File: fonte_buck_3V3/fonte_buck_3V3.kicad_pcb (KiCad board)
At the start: 2 copper layers, 6 parts, among them U1 LM2594M-3.3

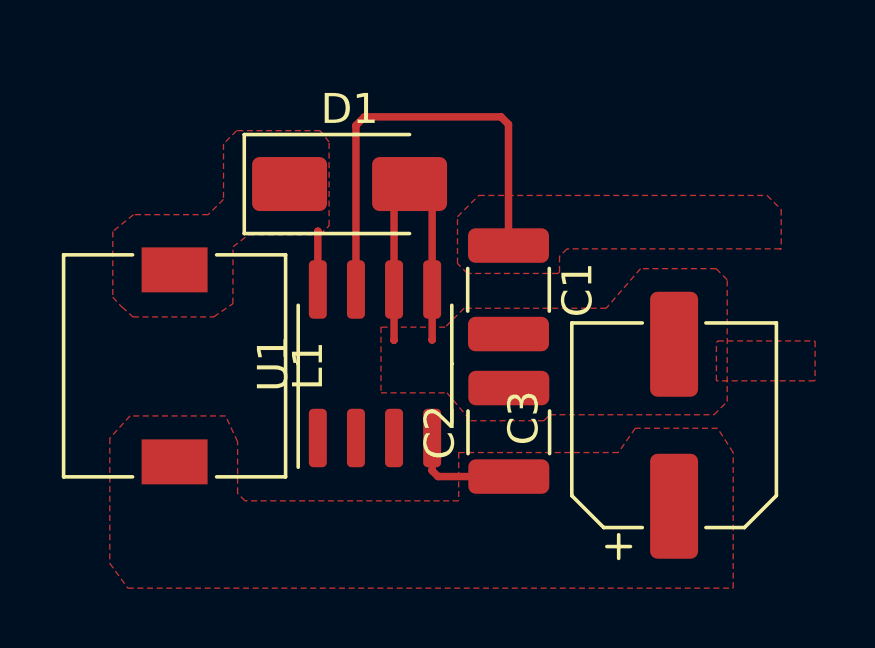
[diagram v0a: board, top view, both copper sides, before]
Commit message: changes in stm and add can module
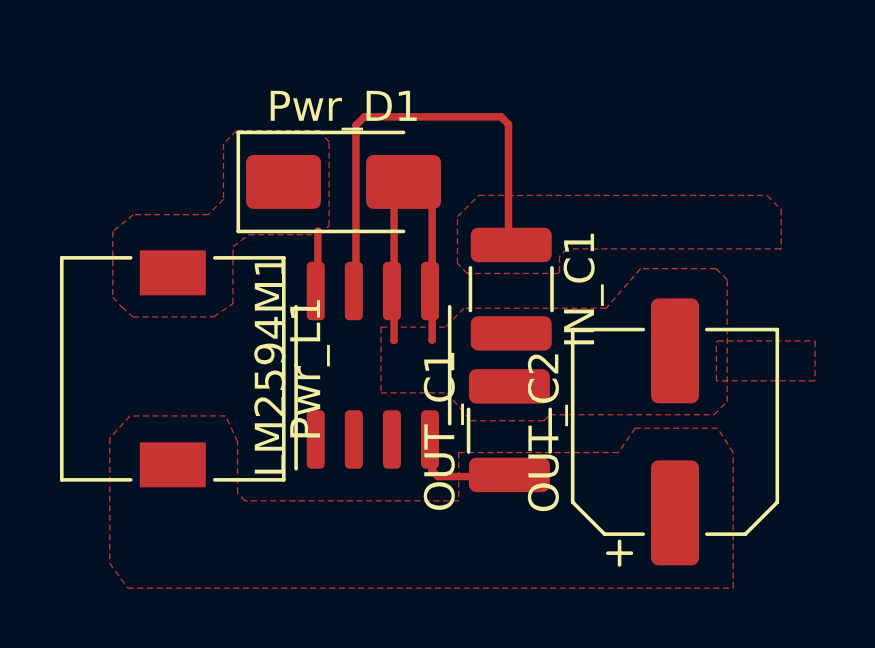
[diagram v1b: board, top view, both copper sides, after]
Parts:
- removed C1: 10uF, Capacitor_SMD:C_1210_3225Metric
- removed C2: 100uF, Capacitor_SMD:C_1210_3225Metric
- removed C3: C, Capacitor_SMD:CP_Elec_6.3x7.7
- removed D1: D, Diode_SMD:D_SMA
- removed L1: 100uH, Inductor_SMD:L_7.3x7.3_H4.5
- removed U1: LM2594M-3.3, Package_SO:SOIC-8_3.9x4.9mm_P1.27mm
- added IN_C1: 10uF, Capacitor_SMD:C_1210_3225Metric, F.Cu at (148.1, 72.5)
- added LM2594M1: LM2594M-3.3, Package_SO:SOIC-8_3.9x4.9mm_P1.27mm, F.Cu at (143.5, 75.0)
- added OUT_C1: 100uF, Capacitor_SMD:C_1210_3225Metric, F.Cu at (148.1, 77.2)
- added OUT_C2: C, Capacitor_SMD:CP_Elec_6.3x7.7, F.Cu at (153.6, 77.2)
- added Pwr_D1: D, Diode_SMD:D_SMA, F.Cu at (142.5, 68.9)
- added Pwr_L1: 100uH, Inductor_SMD:L_7.3x7.3_H4.5, F.Cu at (136.8, 75.1)

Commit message: changes power_supply_buck_5v add layout
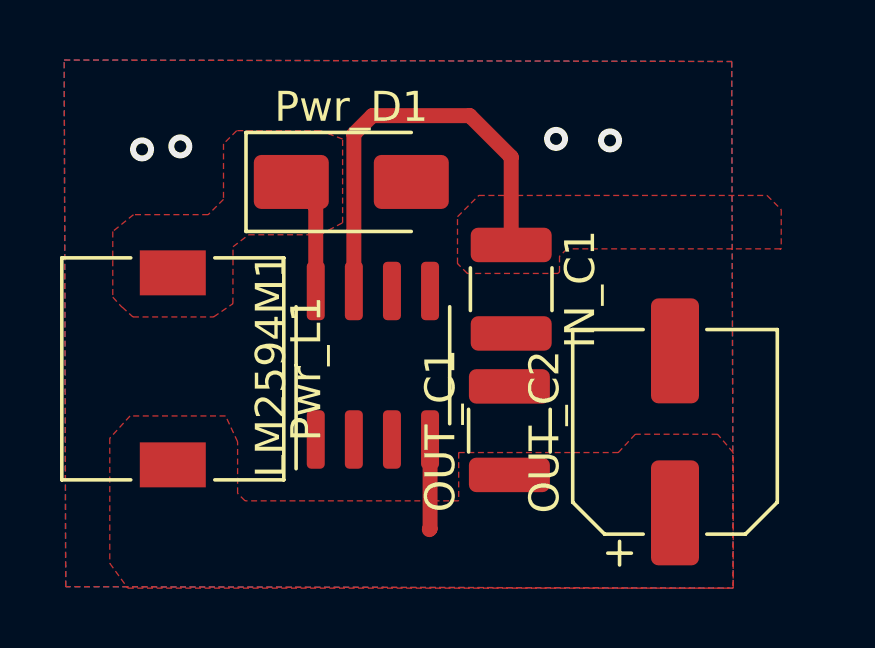
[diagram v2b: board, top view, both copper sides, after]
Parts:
- moved Pwr_D1 0.26 mm to (142.8, 68.9)
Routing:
- net GND: track 10.9 -> 0.00 mm, vias 0 -> 4
- net /Net_diodo: track 1.95 -> 3.97 mm
- net +3V3: track 3.73 -> 3.02 mm
- net +12V: track 14.8 -> 14.2 mm
- added copper zone on B.Cu, net GND
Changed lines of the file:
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@@
   )
   (footprint "Diode_SMD:D_SMA" (layer "F.Cu")
-    (at 142.5425 68.91)
+    (at 142.8 68.91)
     (descr "Diode SMA (DO-214AC)")
     (tags "Diode SMA (DO-214AC)")
@@
     )
   )
-  (segment (start 143.24 66.74) (end 147.79 66.74) (width 0.25) (layer "F.Cu") (net 1))
-  (segment (start 147.79 66.74) (end 148.04 66.99) (width 0.25) (layer "F.Cu") (net 1))
-  (segment (start 142.955 72.495) (end 142.955 67.025) (width 0.25) (layer "F.Cu") (net 1))
-  (segment (start 148.04 66.99) (end 148.04 71.03) (width 0.25) (layer "F.Cu") (net 1))
-  (segment (start 142.955 67.025) (end 143.24 66.74) (width 0.25) (layer "F.Cu") (net 1))
-  (segment (start 145.49 74.18) (end 145.495 74.175) (width 0.25) (layer "F.Cu") (net 2))
-  (segment (start 144.225 74.185) (end 144.22 74.19) (width 0.25) (layer "F.Cu") (net 2))
-  (segment (start 145.495 72.495) (end 145.495 69.7325) (width 0.25) (layer "F.Cu") (net 2))
-  (segment (start 144.225 72.495) (end 144.225 69.4975) (width 0.25) (layer "F.Cu") (net 2))
-  (segment (start 144.225 72.495) (end 144.225 74.185) (width 0.25) (layer "F.Cu") (net 2))
-  (segment (start 145.495 72.495) (end 145.495 74.175) (width 0.25) (layer "F.Cu") (net 2))
-  (segment (start 144.225 69.4975) (end 144.7425 68.98) (width 0.25) (layer "F.Cu") (net 2))
-  (segment (start 145.495 69.7325) (end 144.7425 68.98) (width 0.25) (layer "F.Cu") (net 2))
-  (segment (start 145.495 77.445) (end 145.495 78.535) (width 0.25) (layer "F.Cu") (net 3))
-  (segment (start 145.69 78.73) (end 148.05 78.73) (width 0.25) (layer "F.Cu") (net 3))
-  (segment (start 145.495 78.535) (end 145.69 78.73) (width 0.25) (layer "F.Cu") (net 3))
-  (segment (start 141.685 70.555) (end 141.69 70.55) (width 0.25) (layer "F.Cu") (net 4))
-  (segment (start 141.685 72.495) (end 141.685 70.555) (width 0.25) (layer "F.Cu") (net 4))
+  (segment (start 146.75 66.7) (end 148.13 68.08) (width 0.5) (layer "F.Cu") (net 1))
+  (segment (start 142.885 72.545) (end 142.885 67.315) (width 0.5) (layer "F.Cu") (net 1))
+  (segment (start 143.5 66.7) (end 146.75 66.7) (width 0.5) (layer "F.Cu") (net 1))
+  (segment (start 148.13 68.08) (end 148.13 71.01) (width 0.5) (layer "F.Cu") (net 1))
+  (segment (start 142.885 67.315) (end 143.5 66.7) (width 0.5) (layer "F.Cu") (net 1))
+  (via (at 151.425 67.525) (size 0.8) (drill 0.4) (layers "F.Cu" "B.Cu") (free) (net 2))
+  (via (at 135.825 67.825) (size 0.8) (drill 0.4) (layers "F.Cu" "B.Cu") (free) (net 2))
+  (via (at 149.625 67.475) (size 0.8) (drill 0.4) (layers "F.Cu" "B.Cu") (free) (net 2))
+  (via (at 137.1 67.725) (size 0.8) (drill 0.4) (layers "F.Cu" "B.Cu") (free) (net 2))
+  (segment (start 145.425 77.495) (end 145.425 80.475) (width 0.5) (layer "F.Cu") (net 3))
+  (segment (start 145.425 80.475) (end 145.4 80.5) (width 0.5) (layer "F.Cu") (net 3))
+  (segment (start 141.615 72.545) (end 141.615 69.725) (width 0.5) (layer "F.Cu") (net 4))
+  (segment (start 141.615 69.725) (end 140.8 68.91) (width 0.5) (layer "F.Cu") (net 4))
   (zone (net 4) (net_name "/Net_diodo") (layer "F.Cu") (hatch edge 0.5)
     (priority 1)
     (connect_pads (clearance 0.5))
     (min_thickness 0.25) (filled_areas_thickness no)
-    (fill yes (thermal_gap 0.5) (thermal_bridge_width 0.5))
+    (fill yes (thermal_gap 0.3) (thermal_bridge_width 0.5))
     (polygon
       (pts
@@
         (xy 139.38 70.67)
         (xy 141.76 70.67)
-        (xy 142.06 70.37)
-        (xy 142.06 67.58)
+        (xy 142.51 70.27)
+        (xy 142.51 67.48)
         (xy 141.76 67.2)
         (xy 138.98 67.2)
@@
     )
   )
-  (zone (net 2) (net_name "GND") (layer "F.Cu") (hatch edge 0.5)
-    (priority 4)
-    (connect_pads (clearance 0.5))
-    (min_thickness 0.25) (filled_areas_thickness no)
-    (fill yes (thermal_gap 0.5) (thermal_bridge_width 0.5))
-    (polygon
-      (pts
-        (xy 158.26 74.22)
-        (xy 158.26 75.52)
-        (xy 158.24 75.54)
-        (xy 154.97 75.54)
-        (xy 154.97 74.26)
-        (xy 155.02 74.21)
-        (xy 158.24 74.21)
-        (xy 158.25 74.22)
-      )
-    )
-  )
-  (zone (net 2) (net_name "GND") (layer "F.Cu") (hatch edge 0.5)
-    (priority 2)
-    (connect_pads (clearance 0.5))
-    (min_thickness 0.25) (filled_areas_thickness no)
-    (fill yes (thermal_gap 0.5) (thermal_bridge_width 0.5))
-    (polygon
-      (pts
-        (xy 143.79 73.75)
-        (xy 143.79 75.94)
-        (xy 145.99 75.94)
-        (xy 146.78 76.87)
-        (xy 149.22 76.87)
-        (xy 149.42 76.67)
-        (xy 154.89 76.67)
-        (xy 155.33 76.23)
-        (xy 155.33 72.17)
-        (xy 154.96 71.8)
-        (xy 152.440667 71.8)
-        (xy 151.296666 73.12)
-        (xy 146.56 73.12)
-        (xy 145.93 73.75)
-        (xy 143.78 73.75)
-      )
-    )
-  )
   (zone (net 3) (net_name "+3V3") (layer "F.Cu") (hatch edge 0.5)
+    (priority 1)
     (connect_pads (clearance 0.5))
     (min_thickness 0.25) (filled_areas_thickness no)
@@
         (xy 155.53 82.45)
         (xy 155.53 77.93)
-        (xy 155.01 77.12)
-        (xy 152.267175 77.12)
+        (xy 155.01 77.32)
+        (xy 152.267175 77.32)
         (xy 151.7 77.93)
         (xy 146.379255 77.93)
@@
       )
     )
+  )
+  (zone (net 2) (net_name "GND") (layers "F&B.Cu") (hatch edge 0.5)
+    (connect_pads (clearance 0.5))
+    (min_thickness 0.25) (filled_areas_thickness no)
+    (fill yes (thermal_gap 0.5) (thermal_bridge_width 0.5))
+    (polygon
+      (pts
+        (xy 133.23 64.845)
+        (xy 155.48 64.895)
+        (xy 155.53 82.45)
+        (xy 133.28 82.4)
+      )
+    )
